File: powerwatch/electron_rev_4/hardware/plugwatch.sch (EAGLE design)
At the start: 116 parts, among them J1 DM3AT-SF-PEJM5, J2 TC2030-JLINK-NL, U1 BGA725L6-ALT, U10 SIP32510, U11 SIP32510, U12 SIP32510, U13 SIP32510, U14 MPU-9250, U2 SAFFB1G56KB0F0A, U3 ISL29035, U4 MAX-M8, U5 MAX740XESA, U6 SIP32510, U7 NRF51822QF, U8 OPA322AIDBVT, U9 SIP32510, X1 32.768k, X2 16MHz

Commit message: added power supervisory circuit
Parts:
- added J3, J4: (no value), SparkFun-Connectors:JST_2MM_MALE
- added Q1: SI223DDS, fets:SI223DDS
- added R24: 10.4k, passives:RESISTOR0402_RES
- added R27: 101k, passives:RESISTOR0402_RES
- added SJ1: (no value), jumper:SJW
- added U15: TPS3839G25DBZ, chips:TPS3839G25DBZ
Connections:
- new net !EXTERNAL_RST: ASSY1.RST, Q1.G, U15.!RST
- new net !SOFT_RST: ASSY1.A0, R3.2, S2.P$2
- new net N$23: J3.+, Q1.S, R24.1, SJ1.1
- new net N$30: R24.2, R27.1, U15.VDD
- new net N$35: J4.+, Q1.D, SJ1.2
- net !SAFEMODE: no longer ASSY1.A0, R3.2, S2.P$2
- net GND: now also J3.-, J4.-, R27.2, U15.GND
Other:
- note added: "Battery plugs in here"
- note added: "PFET to gate the system. Add jumper incase reverse diode voltage drop doesn't work as expected with the charging circuit"
- note added: "Power Management"
- note added: "Use jumper cable from board to particle"
- note added: "Voltage supervisor. Triggers at 3.08V. We want to trigger at 3.3V, so voltage divide down with 1% resistors."
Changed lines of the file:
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@@
 </part>
 <part name="GND41" library="supply1" library_urn="urn:adsk.eagle:library:371" deviceset="GND" device=""/>
+<part name="FRAME5" library="lab11-frames" deviceset="LETTER_L_BLANK" device=""/>
+<part name="U15" library="chips" deviceset="TPS3839" device="G25DBZ"/>
+<part name="J3" library="SparkFun-Connectors" deviceset="JST_2MM_MALE" device=""/>
+<part name="J4" library="SparkFun-Connectors" deviceset="JST_2MM_MALE" device=""/>
+<part name="GND13" library="supply1" library_urn="urn:adsk.eagle:library:371" deviceset="GND" device=""/>
+<part name="R24" library="passives" deviceset="RESISTOR" device="0402_RES" value="10.4k">
+<attribute name="DESCRIPTION" value="RES SMD 150 OHM 1% 1/16W 0402"/>
+<attribute name="DIGIKEY" value="RMCF0402FT150RCT-ND"/>
+<attribute name="MANUFACTURER" value="Stackpole Electronics"/>
+<attribute name="MPN" value="RMCF0402FT150R"/>
+</part>
+<part name="R27" library="passives" deviceset="RESISTOR" device="0402_RES" value="101k">
+<attribute name="DESCRIPTION" value="RES SMD 150 OHM 1% 1/16W 0402"/>
+<attribute name="DIGIKEY" value="RMCF0402FT150RCT-ND"/>
+<attribute name="MANUFACTURER" value="Stackpole Electronics"/>
+<attribute name="MPN" value="RMCF0402FT150R"/>
+</part>
+<part name="Q1" library="fets" deviceset="SI223DDS" device=""/>
+<part name="GND39" library="supply1" library_urn="urn:adsk.eagle:library:371" deviceset="GND" device=""/>
+<part name="SJ1" library="jumper" library_urn="urn:adsk.eagle:library:252" deviceset="SJ" device="W" package3d_urn="urn:adsk.eagle:package:15507/1"/>
 </parts>
 <sheets>
+<sheet>
+<description>Power Management</description>
+<plain>
+<text x="236.22" y="182.88" size="1.778" layer="98" align="bottom-center">Power Management</text>
+<text x="60.96" y="134.62" size="1.778" layer="98" align="bottom-center">Battery plugs in here</text>
+<text x="104.14" y="81.28" size="1.778" layer="98" align="bottom-center">Voltage supervisor.
+Triggers at 3.08V.
+We want to trigger at 3.3V, so voltage
+divide down with 1% resistors.</text>
+<text x="116.84" y="144.78" size="1.778" layer="98" align="bottom-center">PFET to gate the system.
+Add jumper incase reverse diode voltage
+drop doesn't work as expected
+with the charging circuit</text>
+<text x="157.48" y="132.08" size="1.778" layer="98" align="bottom-center">Use jumper cable from
+board to particle</text>
+</plain>
+<instances>
+<instance part="FRAME5" gate="G$1" x="0" y="0"/>
+<instance part="FRAME5" gate="G$2" x="152.4" y="0"/>
+<instance part="U15" gate="G$1" x="96.52" y="96.52"/>
+<instance part="J3" gate="G$1" x="63.5" y="124.46" rot="R90"/>
+<instance part="J4" gate="G$1" x="144.78" y="124.46" rot="MR90"/>
+<instance part="GND13" gate="1" x="73.66" y="86.36"/>
+<instance part="R24" gate="G$1" x="83.82" y="116.84" rot="R270">
+<attribute name="DIGIKEY" x="83.82" y="116.84" size="1.27" layer="96" rot="R270" display="off"/>
+</instance>
+<instance part="R27" gate="G$1" x="83.82" y="104.14" rot="R270">
+<attribute name="DIGIKEY" x="83.82" y="104.14" size="1.27" layer="96" rot="R270" display="off"/>
+</instance>
+<instance part="Q1" gate="G$1" x="116.84" y="127" smashed="yes" rot="MR90">
+<attribute name="NAME" x="124.46" y="121.92" size="1.778" layer="95" rot="MR0"/>
+</instance>
+<instance part="GND39" gate="1" x="137.16" y="111.76"/>
+<instance part="SJ1" gate="1" x="116.84" y="137.16"/>
+</instances>
+<busses>
+</busses>
+<nets>
+<net name="GND" class="0">
+<segment>
+<pinref part="GND13" gate="1" pin="GND"/>
+<pinref part="J3" gate="G$1" pin="-"/>
+<wire x1="68.58" y1="124.46" x2="73.66" y2="124.46" width="0.1524" layer="91"/>
+<wire x1="73.66" y1="124.46" x2="73.66" y2="99.06" width="0.1524" layer="91"/>
+<pinref part="U15" gate="G$1" pin="GND"/>
+<wire x1="73.66" y1="99.06" x2="73.66" y2="88.9" width="0.1524" layer="91"/>
+<wire x1="93.98" y1="99.06" x2="83.82" y2="99.06" width="0.1524" layer="91"/>
+<junction x="73.66" y="99.06"/>
+<pinref part="R27" gate="G$1" pin="2"/>
+<wire x1="83.82" y1="99.06" x2="73.66" y2="99.06" width="0.1524" layer="91"/>
+<wire x1="83.82" y1="101.6" x2="83.82" y2="99.06" width="0.1524" layer="91"/>
+<junction x="83.82" y="99.06"/>
+</segment>
+<segment>
+<pinref part="J4" gate="G$1" pin="-"/>
+<wire x1="139.7" y1="124.46" x2="137.16" y2="124.46" width="0.1524" layer="91"/>
+<pinref part="GND39" gate="1" pin="GND"/>
+<wire x1="137.16" y1="124.46" x2="137.16" y2="114.3" width="0.1524" layer="91"/>
+</segment>
+</net>
+<net name="N$23" class="0">
+<segment>
+<pinref part="J3" gate="G$1" pin="+"/>
+<wire x1="68.58" y1="127" x2="83.82" y2="127" width="0.1524" layer="91"/>
+<pinref part="R24" gate="G$1" pin="1"/>
+<wire x1="83.82" y1="121.92" x2="83.82" y2="127" width="0.1524" layer="91"/>
+<junction x="83.82" y="127"/>
+<pinref part="Q1" gate="G$1" pin="S"/>
+<wire x1="83.82" y1="127" x2="106.68" y2="127" width="0.1524" layer="91"/>
+<wire x1="106.68" y1="127" x2="111.76" y2="127" width="0.1524" layer="91"/>
+<wire x1="106.68" y1="127" x2="106.68" y2="137.16" width="0.1524" layer="91"/>
+<junction x="106.68" y="127"/>
+<pinref part="SJ1" gate="1" pin="1"/>
+<wire x1="106.68" y1="137.16" x2="111.76" y2="137.16" width="0.1524" layer="91"/>
+</segment>
+</net>
+<net name="N$30" class="0">
+<segment>
+<pinref part="R24" gate="G$1" pin="2"/>
+<pinref part="R27" gate="G$1" pin="1"/>
+<wire x1="83.82" y1="114.3" x2="83.82" y2="111.76" width="0.1524" layer="91"/>
+<pinref part="U15" gate="G$1" pin="VDD"/>
+<wire x1="83.82" y1="111.76" x2="83.82" y2="109.22" width="0.1524" layer="91"/>
+<wire x1="93.98" y1="104.14" x2="91.44" y2="104.14" width="0.1524" layer="91"/>
+<wire x1="91.44" y1="104.14" x2="91.44" y2="111.76" width="0.1524" layer="91"/>
+<wire x1="91.44" y1="111.76" x2="83.82" y2="111.76" width="0.1524" layer="91"/>
+<junction x="83.82" y="111.76"/>
+</segment>
+</net>
+<net name="!EXTERNAL_RST" class="0">
+<segment>
+<pinref part="U15" gate="G$1" pin="!RST"/>
+<wire x1="109.22" y1="101.6" x2="116.84" y2="101.6" width="0.1524" layer="91"/>
+<pinref part="Q1" gate="G$1" pin="G"/>
+<wire x1="116.84" y1="101.6" x2="116.84" y2="119.38" width="0.1524" layer="91"/>
+<wire x1="116.84" y1="101.6" x2="127" y2="101.6" width="0.1524" layer="91"/>
+<junction x="116.84" y="101.6"/>
+<label x="127" y="101.6" size="1.778" layer="95" xref="yes"/>
+</segment>
+</net>
+<net name="N$35" class="0">
+<segment>
+<pinref part="Q1" gate="G$1" pin="D"/>
+<pinref part="J4" gate="G$1" pin="+"/>
+<wire x1="121.92" y1="127" x2="127" y2="127" width="0.1524" layer="91"/>
+<pinref part="SJ1" gate="1" pin="2"/>
+<wire x1="127" y1="127" x2="139.7" y2="127" width="0.1524" layer="91"/>
+<wire x1="121.92" y1="137.16" x2="127" y2="137.16" width="0.1524" layer="91"/>
+<wire x1="127" y1="137.16" x2="127" y2="127" width="0.1524" layer="91"/>
+<junction x="127" y="127"/>
+</segment>
+</net>
+</nets>
+</sheet>
 <sheet>
 <description>Headers</description>
@@
 <text x="91.44" y="71.12" size="1.778" layer="98">SD Card Adapter</text>
 <text x="93.98" y="160.02" size="3.048" layer="98" align="top-right">Electron headers</text>
-<text x="96.52" y="142.24" size="1.27" layer="104">Note: GPIO choices are arbitrary</text>
+<text x="116.84" y="144.78" size="1.27" layer="104">Note: GPIO choices are arbitrary</text>
 </plain>
 <instances>
@@
 <net name="!SAFEMODE" class="0">
 <segment>
-<pinref part="R3" gate="G$1" pin="2"/>
-<pinref part="S2" gate="G$1" pin="P$2"/>
-<wire x1="160.02" y1="116.84" x2="160.02" y2="119.38" width="0.1524" layer="91"/>
-<wire x1="160.02" y1="119.38" x2="160.02" y2="121.92" width="0.1524" layer="91"/>
-<wire x1="160.02" y1="119.38" x2="162.56" y2="119.38" width="0.1524" layer="91"/>
-<junction x="160.02" y="119.38"/>
-<label x="162.56" y="119.38" size="1.27" layer="95" xref="yes"/>
-</segment>
-<segment>
-<pinref part="ASSY1" gate="A1" pin="A0"/>
-<wire x1="63.5" y1="119.38" x2="60.96" y2="119.38" width="0.1524" layer="91"/>
-<label x="60.96" y="119.38" size="1.27" layer="95" rot="R180" xref="yes"/>
-</segment>
-<segment>
 <pinref part="TP8" gate="G$1" pin="TESTPOINT"/>
 <wire x1="213.36" y1="111.76" x2="210.82" y2="111.76" width="0.1524" layer="91"/>
@@
 </segment>
 </net>
+<net name="!EXTERNAL_RST" class="0">
+<segment>
+<pinref part="ASSY1" gate="A1" pin="RST"/>
+<wire x1="86.36" y1="144.78" x2="93.98" y2="144.78" width="0.1524" layer="91"/>
+<label x="93.98" y="144.78" size="1.27" layer="95" xref="yes"/>
+</segment>
+</net>
+<net name="!SOFT_RST" class="0">
+<segment>
+<pinref part="R3" gate="G$1" pin="2"/>
+<pinref part="S2" gate="G$1" pin="P$2"/>
+<wire x1="160.02" y1="116.84" x2="160.02" y2="119.38" width="0.1524" layer="91"/>
+<wire x1="160.02" y1="119.38" x2="160.02" y2="121.92" width="0.1524" layer="91"/>
+<wire x1="160.02" y1="119.38" x2="162.56" y2="119.38" width="0.1524" layer="91"/>
+<junction x="160.02" y="119.38"/>
+<label x="162.56" y="119.38" size="1.27" layer="95" xref="yes"/>
+</segment>
+<segment>
+<pinref part="ASSY1" gate="A1" pin="A0"/>
+<wire x1="63.5" y1="119.38" x2="60.96" y2="119.38" width="0.1524" layer="91"/>
+<label x="60.96" y="119.38" size="1.27" layer="95" rot="R180" xref="yes"/>
+</segment>
+</net>
 </nets>
 </sheet>
@@
 will not be understood (or retained) with this version.
 </note>
+<note version="8.3" severity="warning">
+Since Version 8.3, EAGLE supports the association of 3D packages
+with devices in libraries, schematics, and board files. Those 3D
+packages will not be understood (or retained) with this version.
+</note>
 </compatibility>

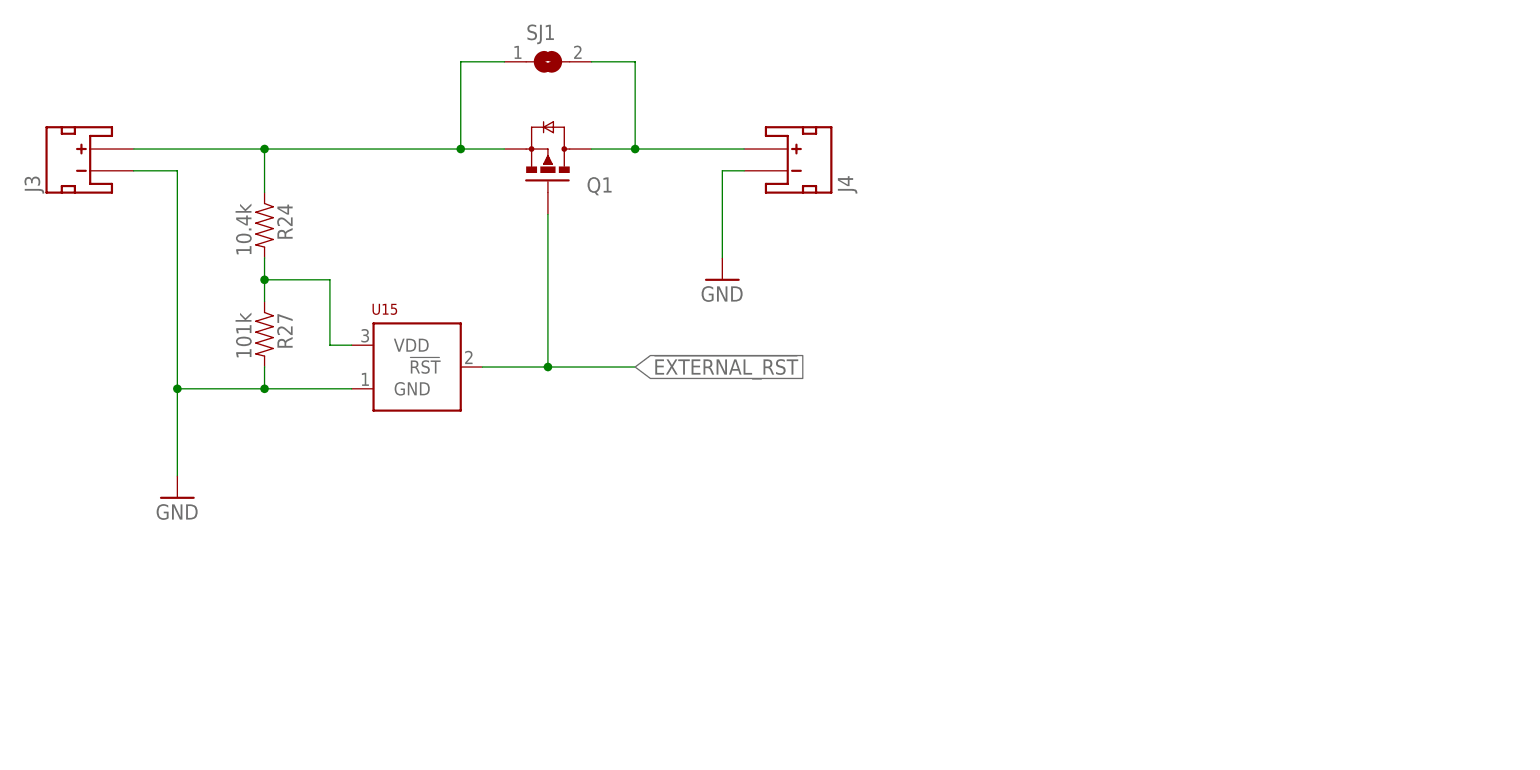
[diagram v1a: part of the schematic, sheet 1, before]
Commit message: change voltage input to also have WDI
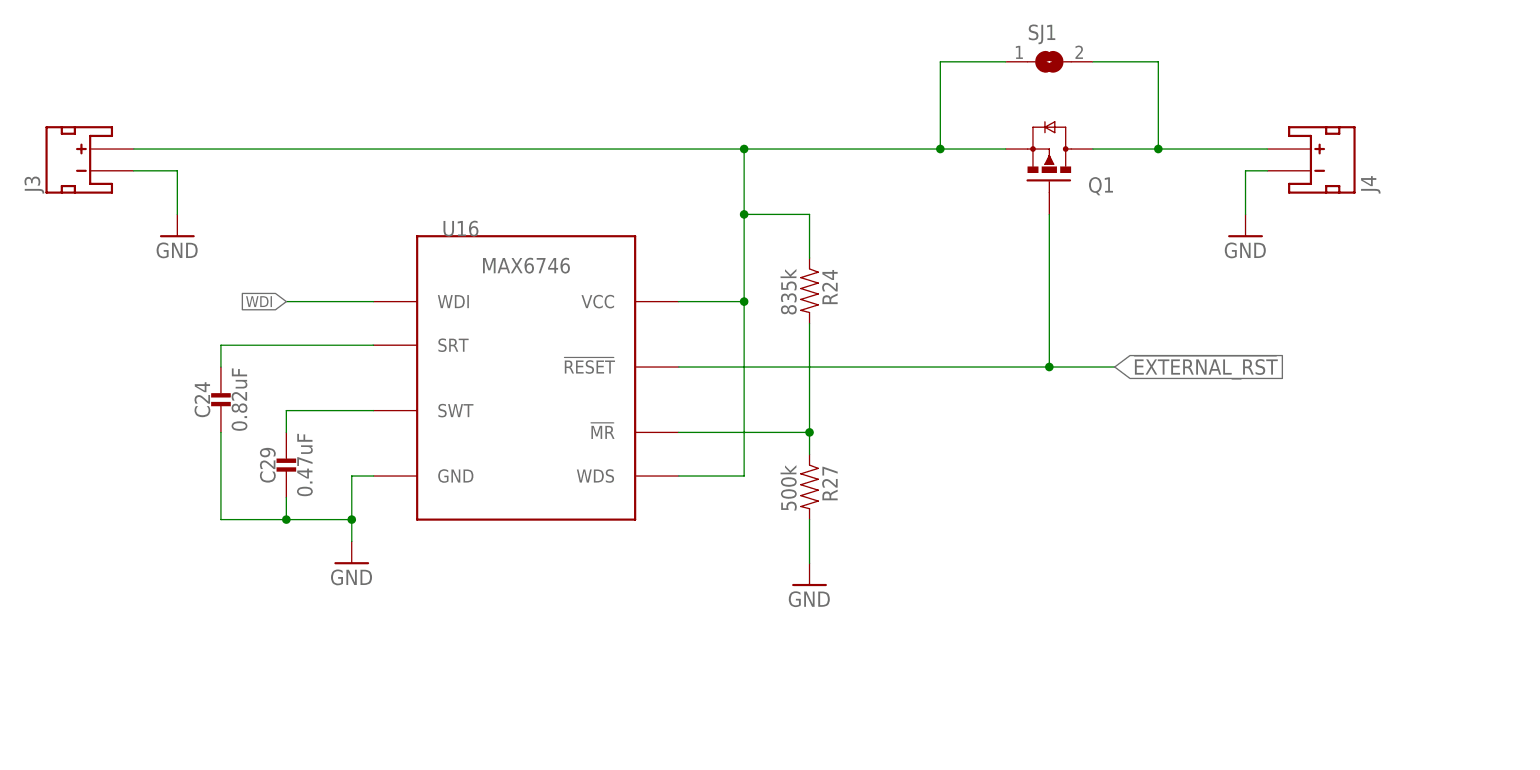
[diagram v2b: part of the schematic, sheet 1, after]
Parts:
- removed U15: TPS3839G25DBZ, chips:TPS3839G25DBZ
- added C24: 0.82uF, passives:CAPACITOR0603_CAP
- added C29: 0.47uF, passives:CAPACITOR0603_CAP
- added U16: MAX6746, chips:MAX6746
- R24: value 10.4k -> 835k
- R27: value 101k -> 500k
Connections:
- removed net N$30: R24.2, R27.1, U15.VDD
- new net N$31: R24.2, R27.1, U16.!MR
- new net N$36: C24.1, U16.SRT
- new net N$39: C29.1, U16.SWT
- new net WDI: ASSY1.DAC, U16.WDI
- net !EXTERNAL_RST: now also U16.!RESET; no longer U15.!RST
- net GND: now also C24.2, C29.2, U16.GND; no longer U15.GND
- net N$23: now also U16.VCC, U16.WDS
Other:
- note added: "Voltage supervisor. MR is the voltage input. MR Triggers at 1.235V. We want to trigger at 3.3V, so voltage divide down with 1% resistors."
- note removed: "Voltage supervisor. Triggers at 3.08V. We want to trigger at 3.3V, so voltage divide down with 1% resistors."
- moved on the sheet: J4, Q1, R24, R27, SJ1
